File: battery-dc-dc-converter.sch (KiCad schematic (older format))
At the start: 18 parts, among them J1 Conn_01x02, J2 Conn_01x02, U1 LMR16030

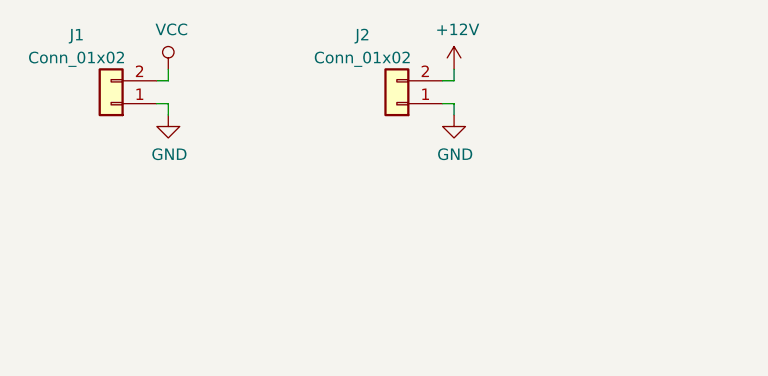
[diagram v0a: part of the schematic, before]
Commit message: Added fuses
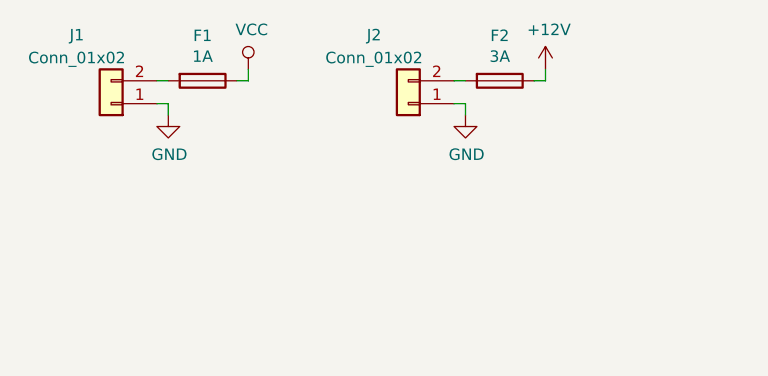
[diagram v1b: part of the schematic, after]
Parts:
- added F1: 1A, Fuse:Fuse_1206_3216Metric_Pad1.42x1.75mm_HandSolder, symbol Device:Fuse
- added F2: 3A, Fuse:Fuse_1206_3216Metric_Pad1.42x1.75mm_HandSolder, symbol Device:Fuse
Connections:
- net +12V: now also F2.1; no longer J2.2 (Pin_2)
- net VCC: now also F1.1; no longer J1.2 (Pin_2)
- new net: F1.2, J1.2 (Pin_2)
- new net: F2.2, J2.2 (Pin_2)
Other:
- moved on the sheet: J2
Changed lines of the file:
@@
 L power:VCC #PWR0109
 U 1 1 5F47FFEF
-P 1250 950
-F 0 "#PWR0109" H 1250 800 50  0001 C CNN
-F 1 "VCC" H 1265 1123 50  0000 C CNN
-F 2 "" H 1250 950 50  0001 C CNN
-F 3 "" H 1250 950 50  0001 C CNN
-	1    1250 950
+P 1600 950
+F 0 "#PWR0109" H 1600 800 50  0001 C CNN
+F 1 "VCC" H 1615 1123 50  0000 C CNN
+F 2 "" H 1600 950 50  0001 C CNN
+F 3 "" H 1600 950 50  0001 C CNN
+	1    1600 950
 	1    0    0    -1
 $EndComp
@@
 L Connector_Generic:Conn_01x02 J2
 U 1 1 5F4E1407
-P 2250 1100
-F 0 "J2" H 2400 800 50  0000 C CNN
-F 1 "Conn_01x02" H 2400 900 50  0000 C CNN
-F 2 "Connector_JST:JST_XH_B2B-XH-A_1x02_P2.50mm_Vertical" H 2250 1100 50  0001 C CNN
-F 3 "~" H 2250 1100 50  0001 C CNN
-F 4 "C8465" H 2250 1100 50  0001 C CNN "LCSC"
-	1    2250 1100
+P 2300 1100
+F 0 "J2" H 2450 800 50  0000 C CNN
+F 1 "Conn_01x02" H 2450 900 50  0000 C CNN
+F 2 "Connector_JST:JST_XH_B2B-XH-A_1x02_P2.50mm_Vertical" H 2300 1100 50  0001 C CNN
+F 3 "~" H 2300 1100 50  0001 C CNN
+F 4 "C8465" H 2300 1100 50  0001 C CNN "LCSC"
+	1    2300 1100
 	-1   0    0    1
 $EndComp
@@
 L power:GND #PWR0111
 U 1 1 5F4E19F6
-P 2500 1150
-F 0 "#PWR0111" H 2500 900 50  0001 C CNN
-F 1 "GND" H 2505 977 50  0000 C CNN
-F 2 "" H 2500 1150 50  0001 C CNN
-F 3 "" H 2500 1150 50  0001 C CNN
-	1    2500 1150
+P 2550 1150
+F 0 "#PWR0111" H 2550 900 50  0001 C CNN
+F 1 "GND" H 2555 977 50  0000 C CNN
+F 2 "" H 2550 1150 50  0001 C CNN
+F 3 "" H 2550 1150 50  0001 C CNN
+	1    2550 1150
 	1    0    0    -1
 $EndComp
@@
 L power:+12V #PWR0112
 U 1 1 5F4E22CD
-P 2500 950
-F 0 "#PWR0112" H 2500 800 50  0001 C CNN
-F 1 "+12V" H 2515 1123 50  0000 C CNN
-F 2 "" H 2500 950 50  0001 C CNN
-F 3 "" H 2500 950 50  0001 C CNN
-	1    2500 950
-	1    0    0    -1
-$EndComp
-Wire Wire Line
-	2450 1000 2500 1000
-Wire Wire Line
-	2500 1000 2500 950
-Wire Wire Line
-	2450 1100 2500 1100
-Wire Wire Line
-	2500 1100 2500 1150
-Wire Wire Line
-	1250 1000 1250 950
+P 2900 950
+F 0 "#PWR0112" H 2900 800 50  0001 C CNN
+F 1 "+12V" H 2915 1123 50  0000 C CNN
+F 2 "" H 2900 950 50  0001 C CNN
+F 3 "" H 2900 950 50  0001 C CNN
+	1    2900 950
+	1    0    0    -1
+$EndComp
+Wire Wire Line
+	2500 1000 2550 1000
+Wire Wire Line
+	2500 1100 2550 1100
+Wire Wire Line
+	2550 1100 2550 1150
 Wire Wire Line
 	1250 1100 1250 1150
@@
 Wire Wire Line
 	7800 3450 8200 3450
+$Comp
+L Device:Fuse F1
+U 1 1 5FB1FA77
+P 1400 1000
+F 0 "F1" V 1203 1000 50  0000 C CNN
+F 1 "1A" V 1294 1000 50  0000 C CNN
+F 2 "Fuse:Fuse_1206_3216Metric_Pad1.42x1.75mm_HandSolder" V 1330 1000 50  0001 C CNN
+F 3 "~" H 1400 1000 50  0001 C CNN
+F 4 "C182305" H 1400 1000 50  0001 C CNN "LCSC"
+	1    1400 1000
+	0    1    1    0
+$EndComp
+Wire Wire Line
+	1550 1000 1600 1000
+Wire Wire Line
+	1600 1000 1600 950
+$Comp
+L Device:Fuse F2
+U 1 1 5FB27E6C
+P 2700 1000
+F 0 "F2" V 2503 1000 50  0000 C CNN
+F 1 "3A" V 2594 1000 50  0000 C CNN
+F 2 "Fuse:Fuse_1206_3216Metric_Pad1.42x1.75mm_HandSolder" V 2630 1000 50  0001 C CNN
+F 3 "~" H 2700 1000 50  0001 C CNN
+F 4 "C182441" H 2700 1000 50  0001 C CNN "LCSC"
+	1    2700 1000
+	0    1    1    0
+$EndComp
+Wire Wire Line
+	2850 1000 2900 1000
+Wire Wire Line
+	2900 1000 2900 950
 $EndSCHEMATC

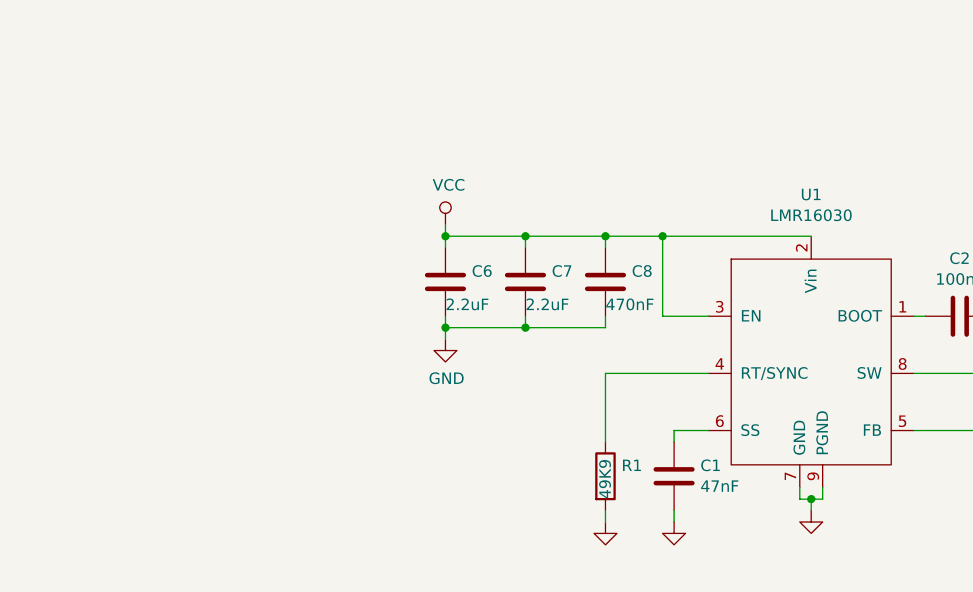
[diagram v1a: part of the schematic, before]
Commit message: Added low voltage protection
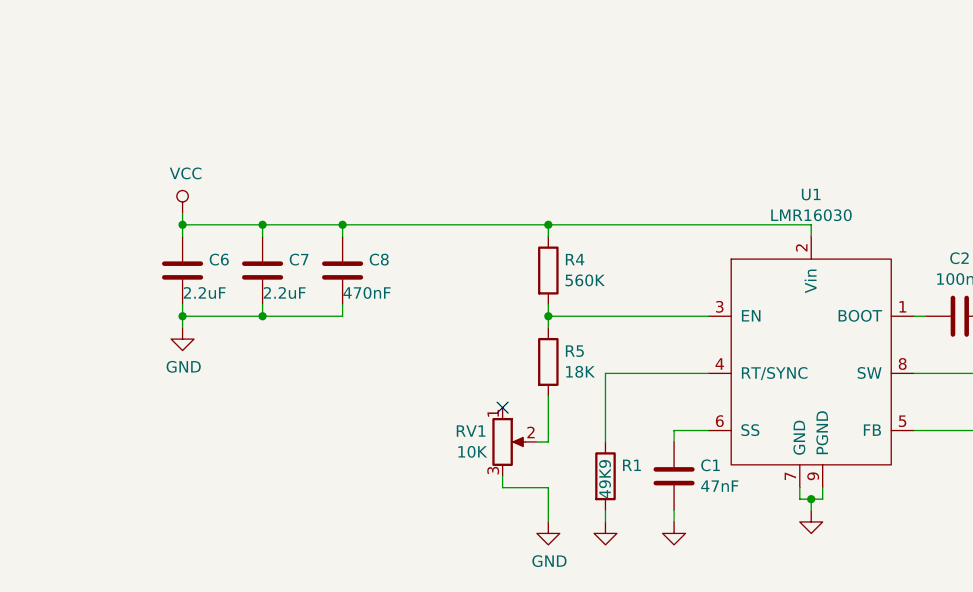
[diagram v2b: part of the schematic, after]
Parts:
- added R4: 560K, Resistor_SMD:R_0805_2012Metric_Pad1.20x1.40mm_HandSolder, symbol Device:R
- added R5: 18K, Resistor_SMD:R_0805_2012Metric_Pad1.20x1.40mm_HandSolder, symbol Device:R
- added RV1: 10K, Potentiometer_THT:Potentiometer_Vishay_T73XX_Horizontal, symbol Device:R_POT
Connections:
- net GND: now also RV1.3
- net VCC: now also R4.1; no longer U1.3 (EN)
- new net: R4.2, R5.1, U1.3 (EN)
- new net: R5.2, RV1.2
- no-connect marks 0 -> 1
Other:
- moved on the sheet: C6, C7, C8
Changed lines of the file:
@@
 Wire Wire Line
 	4000 3700 4450 3700
-Wire Wire Line
-	4450 3450 4250 3450
-Wire Wire Line
-	4250 3450 4250 3100
-Wire Wire Line
-	4250 3100 4900 3100
 $Comp
 L power:VCC #PWR0104
 U 1 1 5F472161
-P 3300 3050
-F 0 "#PWR0104" H 3300 2900 50  0001 C CNN
-F 1 "VCC" H 3315 3223 50  0000 C CNN
-F 2 "" H 3300 3050 50  0001 C CNN
-F 3 "" H 3300 3050 50  0001 C CNN
-	1    3300 3050
-	1    0    0    -1
-$EndComp
-Connection ~ 4250 3100
+P 2150 3000
+F 0 "#PWR0104" H 2150 2850 50  0001 C CNN
+F 1 "VCC" H 2165 3173 50  0000 C CNN
+F 2 "" H 2150 3000 50  0001 C CNN
+F 3 "" H 2150 3000 50  0001 C CNN
+	1    2150 3000
+	1    0    0    -1
+$EndComp
 $Comp
 L Device:D_Shockley D1
@@
 L Device:C C8
 U 1 1 5F4F514D
-P 4000 3300
-F 0 "C8" H 4115 3346 50  0000 L CNN
-F 1 "470nF" H 4000 3200 50  0000 L CNN
-F 2 "Capacitor_SMD:C_0805_2012Metric" H 4038 3150 50  0001 C CNN
-F 3 "~" H 4000 3300 50  0001 C CNN
-F 4 "C13967" H 4000 3300 50  0001 C CNN "LCSC"
-	1    4000 3300
+P 2850 3250
+F 0 "C8" H 2965 3296 50  0000 L CNN
+F 1 "470nF" H 2850 3150 50  0000 L CNN
+F 2 "Capacitor_SMD:C_0805_2012Metric" H 2888 3100 50  0001 C CNN
+F 3 "~" H 2850 3250 50  0001 C CNN
+F 4 "C13967" H 2850 3250 50  0001 C CNN "LCSC"
+	1    2850 3250
 	1    0    0    -1
 $EndComp
@@
 L Device:C C7
 U 1 1 5F4F58E3
-P 3650 3300
-F 0 "C7" H 3765 3346 50  0000 L CNN
-F 1 "2.2uF" H 3650 3200 50  0000 L CNN
-F 2 "Capacitor_SMD:C_1206_3216Metric" H 3688 3150 50  0001 C CNN
-F 3 "~" H 3650 3300 50  0001 C CNN
-F 4 "C50254" H 3650 3300 50  0001 C CNN "LCSC"
-	1    3650 3300
+P 2500 3250
+F 0 "C7" H 2615 3296 50  0000 L CNN
+F 1 "2.2uF" H 2500 3150 50  0000 L CNN
+F 2 "Capacitor_SMD:C_1206_3216Metric" H 2538 3100 50  0001 C CNN
+F 3 "~" H 2500 3250 50  0001 C CNN
+F 4 "C50254" H 2500 3250 50  0001 C CNN "LCSC"
+	1    2500 3250
 	1    0    0    -1
 $EndComp
@@
 L Device:C C6
 U 1 1 5F4F6FC9
-P 3300 3300
-F 0 "C6" H 3415 3346 50  0000 L CNN
-F 1 "2.2uF" H 3300 3200 50  0000 L CNN
-F 2 "Capacitor_SMD:C_1206_3216Metric" H 3338 3150 50  0001 C CNN
-F 3 "~" H 3300 3300 50  0001 C CNN
-F 4 "C50254" H 3300 3300 50  0001 C CNN "LCSC"
-	1    3300 3300
-	1    0    0    -1
-$EndComp
-Wire Wire Line
-	3300 3100 3300 3050
-Wire Wire Line
-	3300 3150 3300 3100
-Connection ~ 3300 3100
-Wire Wire Line
-	3650 3150 3650 3100
-Connection ~ 3650 3100
-Wire Wire Line
-	3650 3100 3300 3100
-Wire Wire Line
-	4000 3150 4000 3100
-Connection ~ 4000 3100
-Wire Wire Line
-	4000 3100 3650 3100
-Wire Wire Line
-	4000 3100 4250 3100
-Wire Wire Line
-	4000 3450 4000 3500
-Wire Wire Line
-	4000 3500 3650 3500
-Wire Wire Line
-	3300 3500 3300 3550
-Wire Wire Line
-	3300 3450 3300 3500
-Connection ~ 3300 3500
-Wire Wire Line
-	3650 3450 3650 3500
-Connection ~ 3650 3500
-Wire Wire Line
-	3650 3500 3300 3500
+P 2150 3250
+F 0 "C6" H 2265 3296 50  0000 L CNN
+F 1 "2.2uF" H 2150 3150 50  0000 L CNN
+F 2 "Capacitor_SMD:C_1206_3216Metric" H 2188 3100 50  0001 C CNN
+F 3 "~" H 2150 3250 50  0001 C CNN
+F 4 "C50254" H 2150 3250 50  0001 C CNN "LCSC"
+	1    2150 3250
+	1    0    0    -1
+$EndComp
+Wire Wire Line
+	2150 3050 2150 3000
+Wire Wire Line
+	2150 3100 2150 3050
+Connection ~ 2150 3050
+Wire Wire Line
+	2500 3100 2500 3050
+Connection ~ 2500 3050
+Wire Wire Line
+	2500 3050 2150 3050
+Wire Wire Line
+	2850 3100 2850 3050
+Connection ~ 2850 3050
+Wire Wire Line
+	2850 3050 2500 3050
+Wire Wire Line
+	2850 3400 2850 3450
+Wire Wire Line
+	2850 3450 2500 3450
+Wire Wire Line
+	2150 3450 2150 3500
+Wire Wire Line
+	2150 3400 2150 3450
+Connection ~ 2150 3450
+Wire Wire Line
+	2500 3400 2500 3450
+Connection ~ 2500 3450
+Wire Wire Line
+	2500 3450 2150 3450
 $Comp
 L power:GND #PWR0113
 U 1 1 5F4FF306
-P 3300 3550
-F 0 "#PWR0113" H 3300 3300 50  0001 C CNN
-F 1 "GND" H 3305 3377 50  0000 C CNN
-F 2 "" H 3300 3550 50  0001 C CNN
-F 3 "" H 3300 3550 50  0001 C CNN
-	1    3300 3550
+P 2150 3500
+F 0 "#PWR0113" H 2150 3250 50  0001 C CNN
+F 1 "GND" H 2155 3327 50  0000 C CNN
+F 2 "" H 2150 3500 50  0001 C CNN
+F 3 "" H 2150 3500 50  0001 C CNN
+	1    2150 3500
 	1    0    0    -1
 $EndComp
@@
 Wire Wire Line
 	2900 1000 2900 950
+$Comp
+L Device:R R4
+U 1 1 5FB4A7D9
+P 3750 3250
+F 0 "R4" H 3820 3296 50  0000 L CNN
+F 1 "560K" H 3820 3205 50  0000 L CNN
+F 2 "Resistor_SMD:R_0805_2012Metric_Pad1.20x1.40mm_HandSolder" V 3680 3250 50  0001 C CNN
+F 3 "~" H 3750 3250 50  0001 C CNN
+F 4 "C15785" H 3750 3250 50  0001 C CNN "LCSC"
+	1    3750 3250
+	1    0    0    -1
+$EndComp
+Wire Wire Line
+	2850 3050 3750 3050
+$Comp
+L power:GND #PWR0114
+U 1 1 5FB512A4
+P 3750 4350
+F 0 "#PWR0114" H 3750 4100 50  0001 C CNN
+F 1 "GND" H 3755 4177 50  0000 C CNN
+F 2 "" H 3750 4350 50  0001 C CNN
+F 3 "" H 3750 4350 50  0001 C CNN
+	1    3750 4350
+	1    0    0    -1
+$EndComp
+$Comp
+L Device:R R5
+U 1 1 5FB5230E
+P 3750 3650
+F 0 "R5" H 3820 3696 50  0000 L CNN
+F 1 "18K" H 3820 3605 50  0000 L CNN
+F 2 "Resistor_SMD:R_0805_2012Metric_Pad1.20x1.40mm_HandSolder" V 3680 3650 50  0001 C CNN
+F 3 "~" H 3750 3650 50  0001 C CNN
+F 4 "C17506" H 3750 3650 50  0001 C CNN "LCSC"
+	1    3750 3650
+	1    0    0    -1
+$EndComp
+Wire Wire Line
+	3750 3450 3750 3400
+Wire Wire Line
+	3750 3450 4450 3450
+Wire Wire Line
+	3750 3500 3750 3450
+Connection ~ 3750 3450
+Wire Wire Line
+	3750 3100 3750 3050
+Connection ~ 3750 3050
+Wire Wire Line
+	3750 3050 4900 3050
+Wire Wire Line
+	4900 3050 4900 3100
+$Comp
+L Device:R_POT RV1
+U 1 1 5FB5C125
+P 3550 4000
+F 0 "RV1" H 3481 4046 50  0000 R CNN
+F 1 "10K" H 3481 3955 50  0000 R CNN
+F 2 "Potentiometer_THT:Potentiometer_Vishay_T73XX_Horizontal" H 3550 4000 50  0001 C CNN
+F 3 "~" H 3550 4000 50  0001 C CNN
+F 4 "C118898" H 3550 4000 50  0001 C CNN "LCSC"
+	1    3550 4000
+	1    0    0    -1
+$EndComp
+NoConn ~ 3550 3850
+Wire Wire Line
+	3700 4000 3750 4000
+Wire Wire Line
+	3750 4000 3750 3800
+Wire Wire Line
+	3550 4150 3550 4200
+Wire Wire Line
+	3550 4200 3750 4200
+Wire Wire Line
+	3750 4200 3750 4350
 $EndSCHEMATC

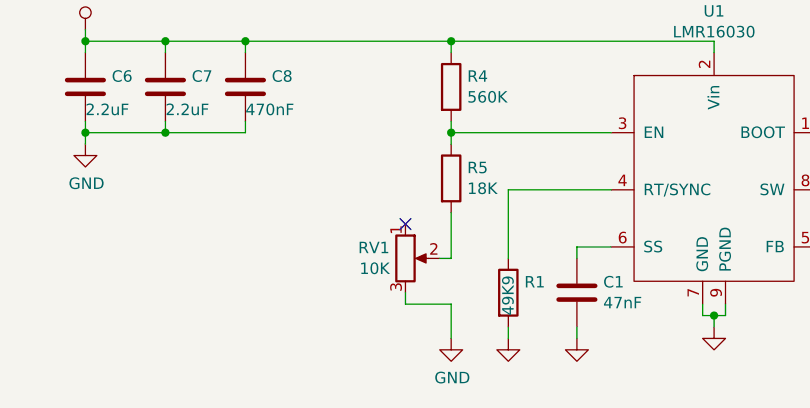
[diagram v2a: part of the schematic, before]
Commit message: Added panelized layout
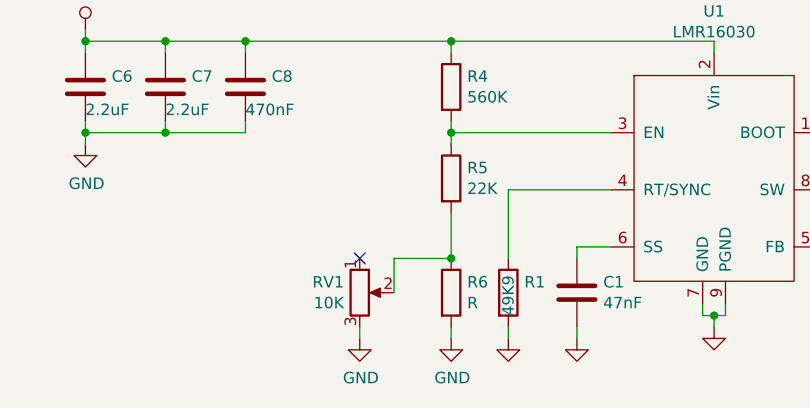
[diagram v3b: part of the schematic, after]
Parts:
- added R6: R, Resistor_SMD:R_0805_2012Metric_Pad1.20x1.40mm_HandSolder, symbol Device:R
- R5: value 18K -> 22K; LCSC C17506 -> C17560
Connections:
- net GND: now also R6.2
- net at R5.2, RV1.2: now also R6.1
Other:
- moved on the sheet: RV1
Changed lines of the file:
@@
 P 3750 3650
 F 0 "R5" H 3820 3696 50  0000 L CNN
-F 1 "18K" H 3820 3605 50  0000 L CNN
+F 1 "22K" H 3820 3605 50  0000 L CNN
 F 2 "Resistor_SMD:R_0805_2012Metric_Pad1.20x1.40mm_HandSolder" V 3680 3650 50  0001 C CNN
 F 3 "~" H 3750 3650 50  0001 C CNN
-F 4 "C17506" H 3750 3650 50  0001 C CNN "LCSC"
+F 4 "C17560" H 3750 3650 50  0001 C CNN "LCSC"
 	1    3750 3650
 	1    0    0    -1
@@
 L Device:R_POT RV1
 U 1 1 5FB5C125
-P 3550 4000
-F 0 "RV1" H 3481 4046 50  0000 R CNN
-F 1 "10K" H 3481 3955 50  0000 R CNN
-F 2 "Potentiometer_THT:Potentiometer_Vishay_T73XX_Horizontal" H 3550 4000 50  0001 C CNN
-F 3 "~" H 3550 4000 50  0001 C CNN
-F 4 "C118898" H 3550 4000 50  0001 C CNN "LCSC"
-	1    3550 4000
+P 3350 4150
+F 0 "RV1" H 3281 4196 50  0000 R CNN
+F 1 "10K" H 3281 4105 50  0000 R CNN
+F 2 "Potentiometer_THT:Potentiometer_Vishay_T73XX_Horizontal" H 3350 4150 50  0001 C CNN
+F 3 "~" H 3350 4150 50  0001 C CNN
+F 4 "C118898" H 3350 4150 50  0001 C CNN "LCSC"
+	1    3350 4150
 	1    0    0    -1
 $EndComp
-NoConn ~ 3550 3850
-Wire Wire Line
-	3700 4000 3750 4000
+NoConn ~ 3350 4000
 Wire Wire Line
 	3750 4000 3750 3800
+$Comp
+L Device:R R6
+U 1 1 5FB76917
+P 3750 4150
+F 0 "R6" H 3820 4196 50  0000 L CNN
+F 1 "R" H 3820 4105 50  0000 L CNN
+F 2 "Resistor_SMD:R_0805_2012Metric_Pad1.20x1.40mm_HandSolder" V 3680 4150 50  0001 C CNN
+F 3 "~" H 3750 4150 50  0001 C CNN
+F 4 "C17477" H 3750 4150 50  0001 C CNN "LCSC"
+	1    3750 4150
+	1    0    0    -1
+$EndComp
+Connection ~ 3750 4000
 Wire Wire Line
-	3550 4150 3550 4200
+	3500 4000 3500 4150
 Wire Wire Line
-	3550 4200 3750 4200
+	3500 4000 3750 4000
+$Comp
+L power:GND #PWR0115
+U 1 1 5FB7F217
+P 3350 4350
+F 0 "#PWR0115" H 3350 4100 50  0001 C CNN
+F 1 "GND" H 3355 4177 50  0000 C CNN
+F 2 "" H 3350 4350 50  0001 C CNN
+F 3 "" H 3350 4350 50  0001 C CNN
+	1    3350 4350
+	1    0    0    -1
+$EndComp
 Wire Wire Line
-	3750 4200 3750 4350
+	3750 4300 3750 4350
+Wire Wire Line
+	3350 4350 3350 4300
 $EndSCHEMATC

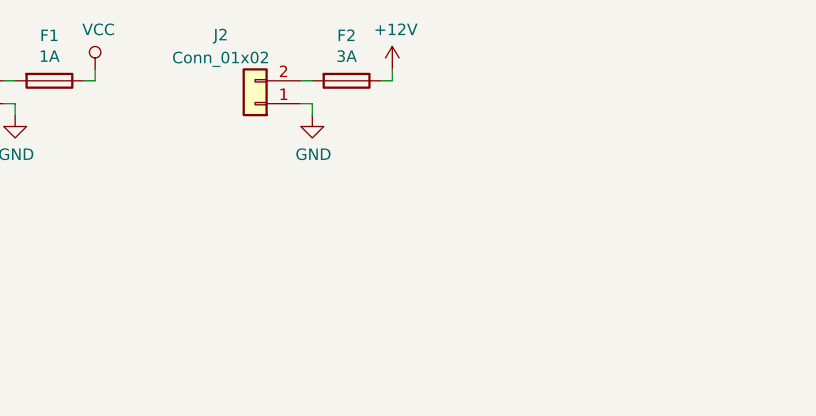
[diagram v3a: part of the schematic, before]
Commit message: Updateed power pads, on/off resistors.
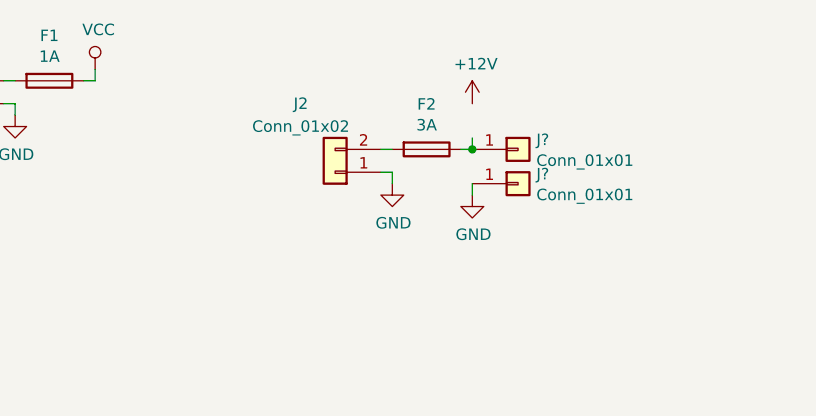
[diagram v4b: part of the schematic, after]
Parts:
- added J? (x2): Conn_01x01, Connector_Wire:SolderWirePad_1x01_SMD_5x10mm, symbol Connector_Generic:Conn_01x01
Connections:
- net +12V: no longer F2.1
- net GND: now also J?.1 (Pin_1)
- new net: F2.1, J?.1 (Pin_1)
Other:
- moved on the sheet: F2, J2
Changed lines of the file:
@@
 L Connector_Generic:Conn_01x02 J2
 U 1 1 5F4E1407
-P 2300 1100
-F 0 "J2" H 2450 800 50  0000 C CNN
-F 1 "Conn_01x02" H 2450 900 50  0000 C CNN
-F 2 "Connector_JST:JST_XH_B2B-XH-A_1x02_P2.50mm_Vertical" H 2300 1100 50  0001 C CNN
-F 3 "~" H 2300 1100 50  0001 C CNN
-F 4 "C8465" H 2300 1100 50  0001 C CNN "LCSC"
-	1    2300 1100
+P 2650 1400
+F 0 "J2" H 2800 1100 50  0000 C CNN
+F 1 "Conn_01x02" H 2800 1200 50  0000 C CNN
+F 2 "Connector_JST:JST_XH_B2B-XH-A_1x02_P2.50mm_Vertical" H 2650 1400 50  0001 C CNN
+F 3 "~" H 2650 1400 50  0001 C CNN
+F 4 "C8465" H 2650 1400 50  0001 C CNN "LCSC"
+	1    2650 1400
 	-1   0    0    1
 $EndComp
@@
 L power:GND #PWR0111
 U 1 1 5F4E19F6
-P 2550 1150
-F 0 "#PWR0111" H 2550 900 50  0001 C CNN
-F 1 "GND" H 2555 977 50  0000 C CNN
-F 2 "" H 2550 1150 50  0001 C CNN
-F 3 "" H 2550 1150 50  0001 C CNN
-	1    2550 1150
+P 2900 1450
+F 0 "#PWR0111" H 2900 1200 50  0001 C CNN
+F 1 "GND" H 2905 1277 50  0000 C CNN
+F 2 "" H 2900 1450 50  0001 C CNN
+F 3 "" H 2900 1450 50  0001 C CNN
+	1    2900 1450
 	1    0    0    -1
 $EndComp
@@
 L power:+12V #PWR0112
 U 1 1 5F4E22CD
-P 2900 950
-F 0 "#PWR0112" H 2900 800 50  0001 C CNN
-F 1 "+12V" H 2915 1123 50  0000 C CNN
-F 2 "" H 2900 950 50  0001 C CNN
-F 3 "" H 2900 950 50  0001 C CNN
-	1    2900 950
-	1    0    0    -1
-$EndComp
-Wire Wire Line
-	2500 1000 2550 1000
-Wire Wire Line
-	2500 1100 2550 1100
-Wire Wire Line
-	2550 1100 2550 1150
+P 3250 1100
+F 0 "#PWR0112" H 3250 950 50  0001 C CNN
+F 1 "+12V" H 3265 1273 50  0000 C CNN
+F 2 "" H 3250 1100 50  0001 C CNN
+F 3 "" H 3250 1100 50  0001 C CNN
+	1    3250 1100
+	1    0    0    -1
+$EndComp
+Wire Wire Line
+	2850 1300 2900 1300
+Wire Wire Line
+	2850 1400 2900 1400
+Wire Wire Line
+	2900 1400 2900 1450
 Wire Wire Line
 	1250 1100 1250 1150
@@
 L Device:Fuse F2
 U 1 1 5FB27E6C
-P 2700 1000
-F 0 "F2" V 2503 1000 50  0000 C CNN
-F 1 "3A" V 2594 1000 50  0000 C CNN
-F 2 "Fuse:Fuse_1206_3216Metric_Pad1.42x1.75mm_HandSolder" V 2630 1000 50  0001 C CNN
-F 3 "~" H 2700 1000 50  0001 C CNN
-F 4 "C182441" H 2700 1000 50  0001 C CNN "LCSC"
-	1    2700 1000
+P 3050 1300
+F 0 "F2" V 2853 1300 50  0000 C CNN
+F 1 "3A" V 2944 1300 50  0000 C CNN
+F 2 "Fuse:Fuse_1206_3216Metric_Pad1.42x1.75mm_HandSolder" V 2980 1300 50  0001 C CNN
+F 3 "~" H 3050 1300 50  0001 C CNN
+F 4 "C182441" H 3050 1300 50  0001 C CNN "LCSC"
+	1    3050 1300
 	0    1    1    0
 $EndComp
 Wire Wire Line
-	2850 1000 2900 1000
-Wire Wire Line
-	2900 1000 2900 950
+	3200 1300 3250 1300
+Wire Wire Line
+	3250 1300 3250 1250
 $Comp
 L Device:R R4
@@
 Wire Wire Line
 	3350 4350 3350 4300
+$Comp
+L Connector_Generic:Conn_01x01 J?
+U 1 1 60369738
+P 3450 1300
+F 0 "J?" H 3530 1342 50  0000 L CNN
+F 1 "Conn_01x01" H 3530 1251 50  0000 L CNN
+F 2 "Connector_Wire:SolderWirePad_1x01_SMD_5x10mm" H 3450 1300 50  0001 C CNN
+F 3 "~" H 3450 1300 50  0001 C CNN
+	1    3450 1300
+	1    0    0    -1
+$EndComp
+Connection ~ 3250 1300
+$Comp
+L Connector_Generic:Conn_01x01 J?
+U 1 1 60369BF3
+P 3450 1450
+F 0 "J?" H 3530 1492 50  0000 L CNN
+F 1 "Conn_01x01" H 3530 1401 50  0000 L CNN
+F 2 "Connector_Wire:SolderWirePad_1x01_SMD_5x10mm" H 3450 1450 50  0001 C CNN
+F 3 "~" H 3450 1450 50  0001 C CNN
+	1    3450 1450
+	1    0    0    -1
+$EndComp
+$Comp
+L power:GND #PWR?
+U 1 1 6036A147
+P 3250 1500
+F 0 "#PWR?" H 3250 1250 50  0001 C CNN
+F 1 "GND" H 3255 1327 50  0000 C CNN
+F 2 "" H 3250 1500 50  0001 C CNN
+F 3 "" H 3250 1500 50  0001 C CNN
+	1    3250 1500
+	1    0    0    -1
+$EndComp
+Wire Wire Line
+	3250 1500 3250 1450
 $EndSCHEMATC
